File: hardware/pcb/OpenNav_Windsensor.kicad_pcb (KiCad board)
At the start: 2 copper layers, 40 x 40 mm, 11 parts, among them IC1 AS5600-ASOT, J1 Conn_01x02_Pin, U1 XIAO-ESP32-C6, U2 StpDwnE3.3-0.5, U3 SS411P, U4 DS18B20

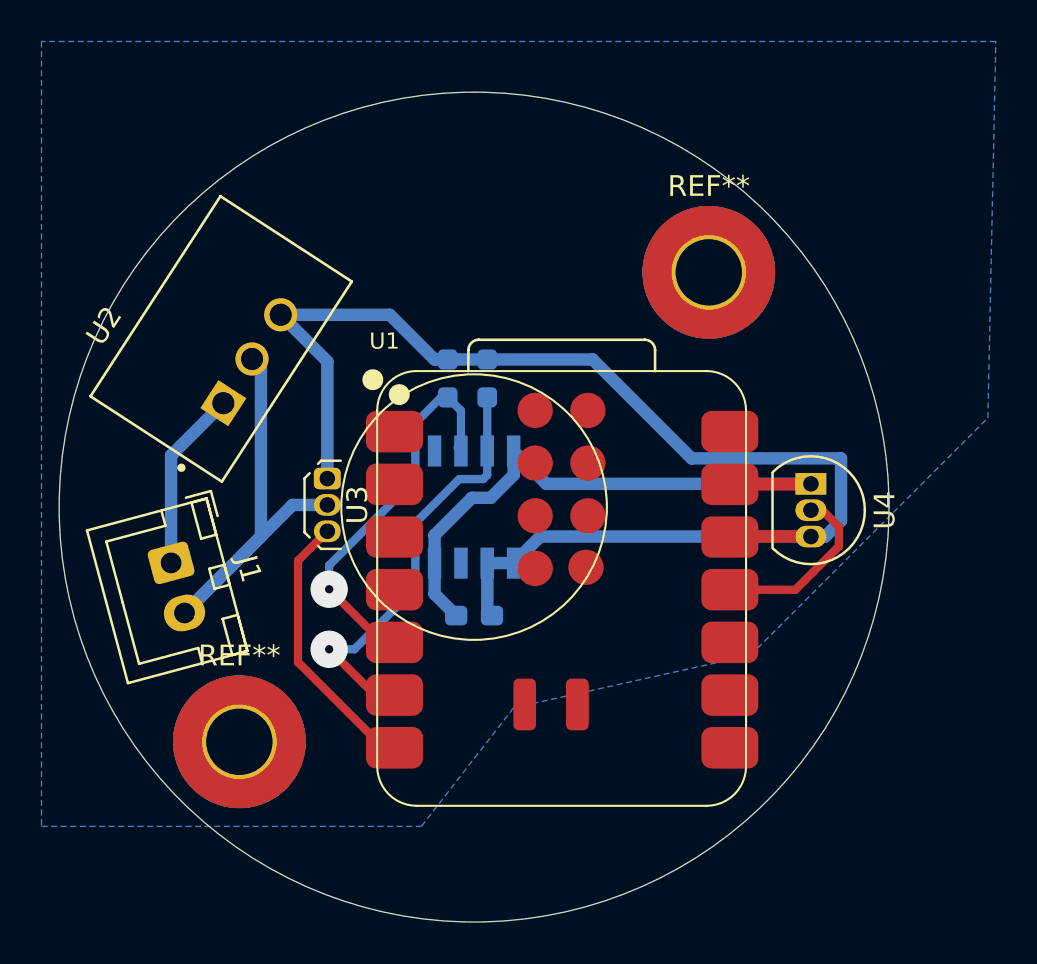
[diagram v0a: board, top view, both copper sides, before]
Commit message: Corrected component sizes and added teardrops
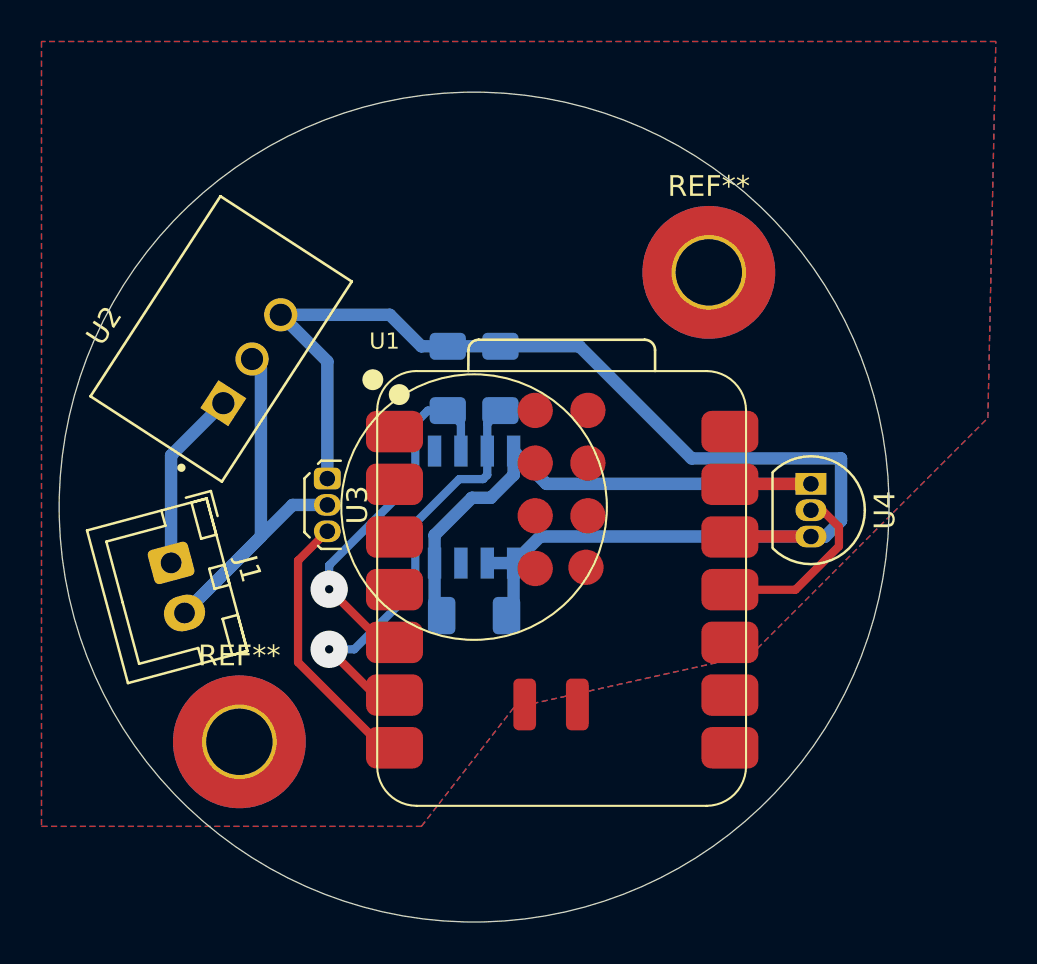
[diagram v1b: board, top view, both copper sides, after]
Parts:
- C3: footprint Capacitor_SMD:C_0603_1608Metric_Pad1.08x0.95mm_HandSolder -> Capacitor_SMD:C_1206_3216Metric_Pad1.33x1.80mm_HandSolder
- R1, R2: footprint Resistor_SMD:R_0603_1608Metric_Pad0.98x0.95mm_HandSolder -> Resistor_SMD:R_1206_3216Metric_Pad1.30x1.75mm_HandSolder
- moved R2 0.64 mm to (134.0, 50.8)
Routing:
- net Net-(IC1-SDA): track 19.5 -> 18.0 mm
- net GND: track 53.3 -> 52.1 mm
- added copper zone on F.Cu, net GND
